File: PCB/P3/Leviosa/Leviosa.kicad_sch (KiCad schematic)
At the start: 56 parts, among them J1 Barrel_Jack, J2 2.54mm 1x03 Spare, Q1 NCE0110K, U1 SS495A, U2 MCP6001R, U3 LM393, U4 MX27517, U5 INA199xxDCK (50V/V)

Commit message: Board revised
- Big change from the last so have a look over
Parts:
- D3: footprint Diode_SMD:D_SMA -> Diode_SMD:D_SOD-323
- renumbered R_shunt1 to R11, R11 to R12, R12 to R13, R13 to R14, R14 to R15, Fault1 to TP_F, U_Ilim1 to U1, V_reg1 to U2, U1 to U3, U2 to U4, U3 to U5, U4 to U6, U5 to U7
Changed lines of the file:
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@@
 		(on_board yes)
 		(dnp no)
-		(property "Reference" "R12"
+		(property "Reference" "R13"
 			(at 216.154 60.198 90)
 			(effects
@@
 			(project "Leviosa"
 				(path "/fe766911-203b-467c-b704-d4bd488f6c98"
-					(reference "R12")
+					(reference "R13")
 					(unit 1)
 				)
@@
 		(dnp no)
 		(property "Reference" "C11"
-			(at 247.65 49.53 90)
+			(at 248.92 49.53 90)
 			(effects
 				(font
@@
 		)
 		(property "Value" "0.1µF"
-			(at 247.65 46.99 90)
+			(at 248.92 46.99 90)
 			(effects
 				(font
@@
 		(on_board yes)
 		(dnp no)
-		(property "Reference" "R_shunt1"
+		(property "Reference" "R11"
 			(at 201.676 60.706 0)
 			(effects
@@
 			(project "Leviosa"
 				(path "/fe766911-203b-467c-b704-d4bd488f6c98"
-					(reference "R_shunt1")
+					(reference "R11")
 					(unit 1)
 				)
@@
 		(on_board yes)
 		(dnp no)
-		(property "Reference" "U5"
+		(property "Reference" "U7"
 			(at 256.286 65.278 0)
 			(effects
@@
 			(project ""
 				(path "/fe766911-203b-467c-b704-d4bd488f6c98"
-					(reference "U5")
+					(reference "U7")
 					(unit 1)
 				)
@@
 		(on_board yes)
 		(dnp no)
-		(property "Reference" "R11"
+		(property "Reference" "R12"
 			(at 209.55 105.41 90)
 			(effects
@@
 			(project "Leviosa"
 				(path "/fe766911-203b-467c-b704-d4bd488f6c98"
-					(reference "R11")
+					(reference "R12")
 					(unit 1)
 				)
@@
 		(on_board yes)
 		(dnp no)
-		(property "Reference" "U_Ilim1"
+		(property "Reference" "U1"
 			(at 43.18 41.91 0)
 			(effects
@@
 			(project "Leviosa"
 				(path "/fe766911-203b-467c-b704-d4bd488f6c98"
-					(reference "U_Ilim1")
+					(reference "U1")
 					(unit 1)
 				)
@@
 		(on_board yes)
 		(dnp no)
-		(property "Reference" "U2"
+		(property "Reference" "U4"
 			(at 150.114 115.062 0)
 			(effects
@@
 			(project ""
 				(path "/fe766911-203b-467c-b704-d4bd488f6c98"
-					(reference "U2")
+					(reference "U4")
 					(unit 1)
 				)
@@
 		(dnp no)
 		(fields_autoplaced yes)
-		(property "Reference" "V_reg1"
+		(property "Reference" "U2"
 			(at 80.01 31.75 0)
 			(effects
@@
 			(project ""
 				(path "/fe766911-203b-467c-b704-d4bd488f6c98"
-					(reference "V_reg1")
+					(reference "U2")
 					(unit 1)
 				)
@@
 		(on_board yes)
 		(dnp no)
-		(property "Reference" "U1"
+		(property "Reference" "U3"
 			(at 128.27 130.81 0)
 			(effects
@@
 			(project "Leviosa"
 				(path "/fe766911-203b-467c-b704-d4bd488f6c98"
-					(reference "U1")
+					(reference "U3")
 					(unit 1)
 				)
@@
 		(on_board yes)
 		(dnp no)
-		(property "Reference" "U4"
+		(property "Reference" "U6"
 			(at 228.092 110.744 0)
 			(effects
@@
 			(project ""
 				(path "/fe766911-203b-467c-b704-d4bd488f6c98"
-					(reference "U4")
+					(reference "U6")
 					(unit 1)
 				)
@@
 			)
 		)
-		(property "Footprint" "Diode_SMD:D_SMA"
+		(property "Footprint" "Diode_SMD:D_SOD-323"
 			(at 191.135 50.8 0)
 			(effects
@@
 		(on_board yes)
 		(dnp no)
-		(property "Reference" "Fault1"
+		(property "Reference" "TP_F"
 			(at 66.04 50.8 0)
 			(effects
@@
 			(project "Leviosa"
 				(path "/fe766911-203b-467c-b704-d4bd488f6c98"
-					(reference "Fault1")
+					(reference "TP_F")
 					(unit 1)
 				)
@@
 		(on_board yes)
 		(dnp no)
-		(property "Reference" "U3"
+		(property "Reference" "U5"
 			(at 193.04 135.89 90)
 			(effects
@@
 			(project ""
 				(path "/fe766911-203b-467c-b704-d4bd488f6c98"
-					(reference "U3")
+					(reference "U5")
 					(unit 2)
 				)
@@
 		(on_board yes)
 		(dnp no)
-		(property "Reference" "R13"
+		(property "Reference" "R14"
 			(at 215.9 69.85 90)
 			(effects
@@
 			(project "Leviosa"
 				(path "/fe766911-203b-467c-b704-d4bd488f6c98"
-					(reference "R13")
+					(reference "R14")
 					(unit 1)
 				)
@@
 		(on_board yes)
 		(dnp no)
-		(property "Reference" "U3"
+		(property "Reference" "U5"
 			(at 177.8 123.19 0)
 			(effects
@@
 			(project ""
 				(path "/fe766911-203b-467c-b704-d4bd488f6c98"
-					(reference "U3")
+					(reference "U5")
 					(unit 3)
 				)
@@
 		(on_board yes)
 		(dnp no)
-		(property "Reference" "R14"
+		(property "Reference" "R15"
 			(at 243.84 93.98 0)
 			(effects
@@
 			(project "Leviosa"
 				(path "/fe766911-203b-467c-b704-d4bd488f6c98"
-					(reference "R14")
+					(reference "R15")
 					(unit 1)
 				)
@@
 		(on_board yes)
 		(dnp no)
-		(property "Reference" "U3"
+		(property "Reference" "U5"
 			(at 193.04 111.252 90)
 			(effects
@@
 			(project ""
 				(path "/fe766911-203b-467c-b704-d4bd488f6c98"
-					(reference "U3")
+					(reference "U5")
 					(unit 1)
 				)

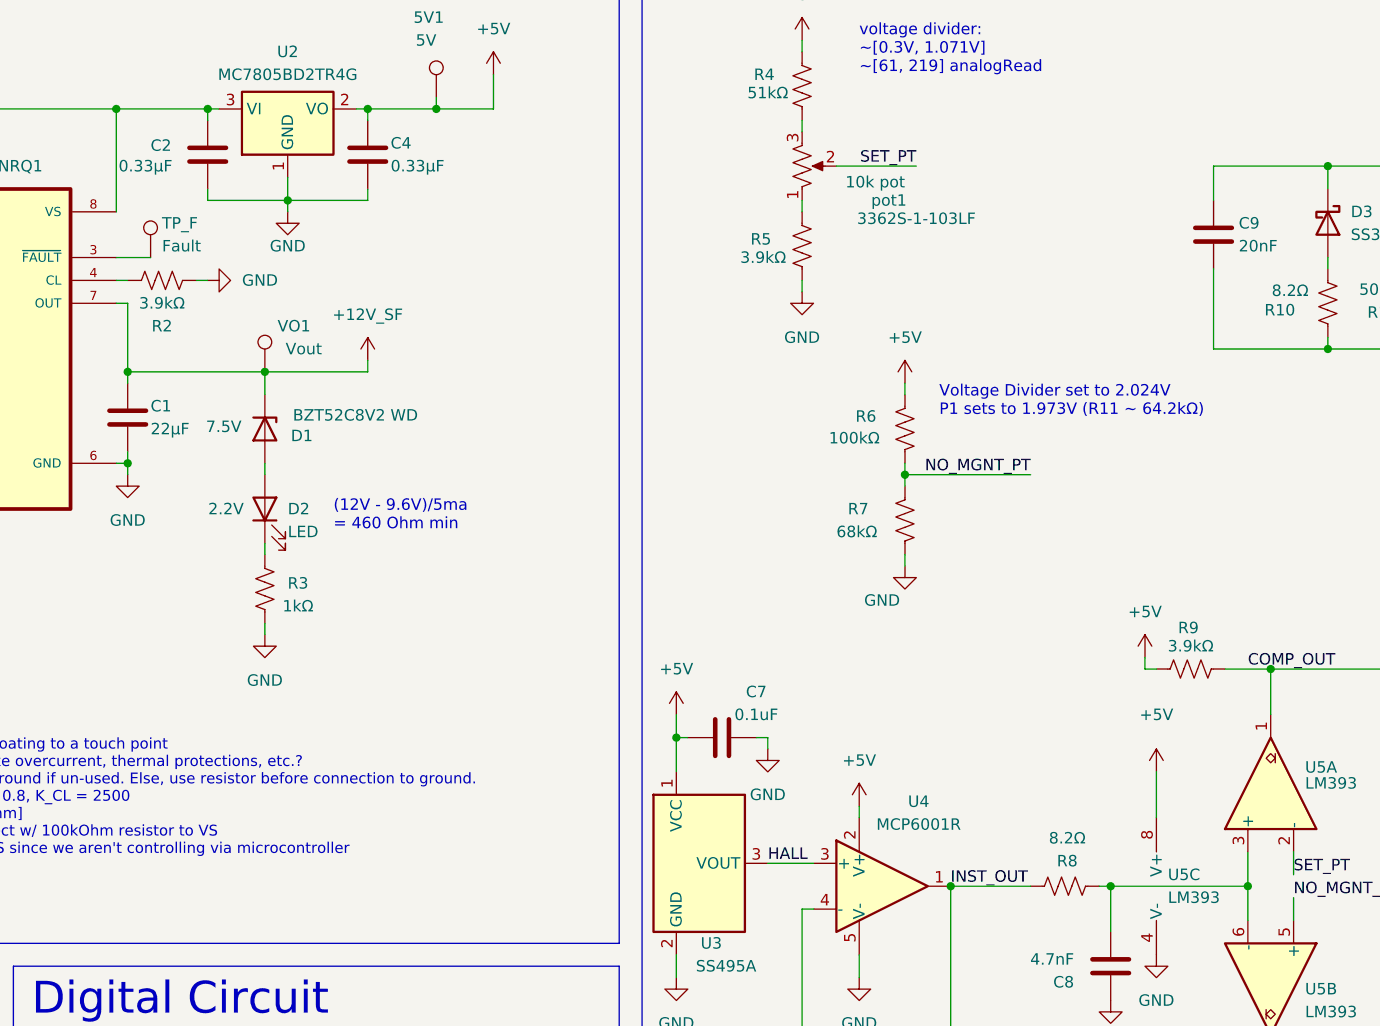
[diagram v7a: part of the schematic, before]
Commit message: added status led for coil and moved components groups closer together
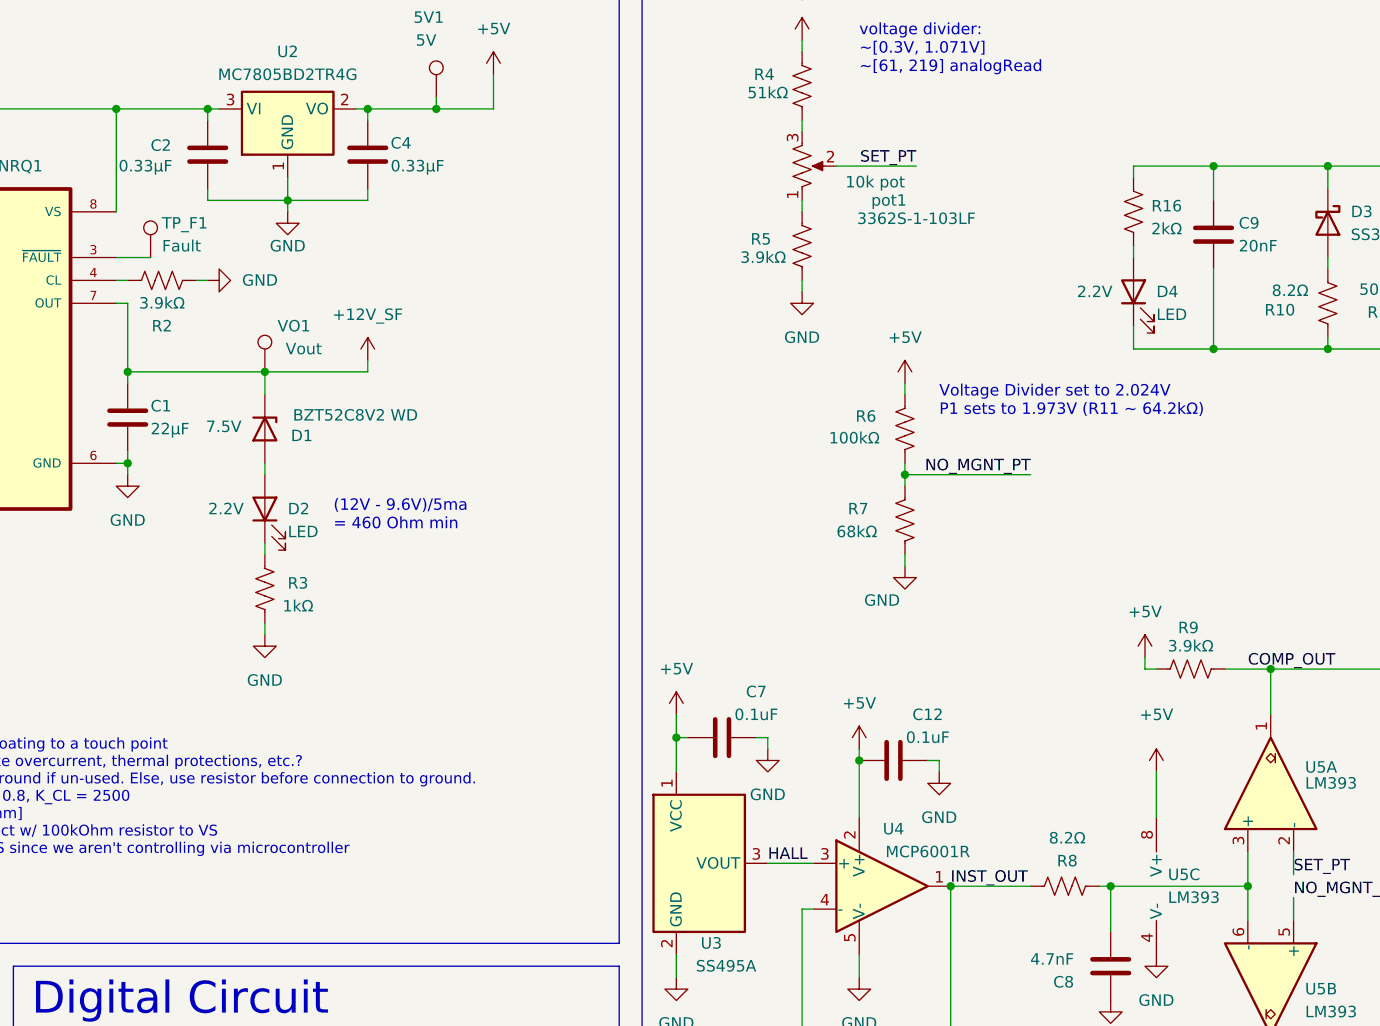
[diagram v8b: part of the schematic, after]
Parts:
- added C12: 0.1uF, Capacitor_SMD:C_0603_1608Metric, symbol Device:C
- added D4: LED, LED_SMD:LED_0805_2012Metric, symbol Device:LED
- added R16: 2kΩ, Resistor_SMD:R_0603_1608Metric, symbol Device:R_US
- renumbered TP_F to TP_F1
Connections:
- net +12V_SF: now also R16.1
- net +5V: now also C12.1
- net COIL_OUT: now also D4.1 (K)
- net GND: now also C12.2
- new net: D4.2 (A), R16.2
